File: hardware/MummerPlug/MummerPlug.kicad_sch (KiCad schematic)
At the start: 8 parts

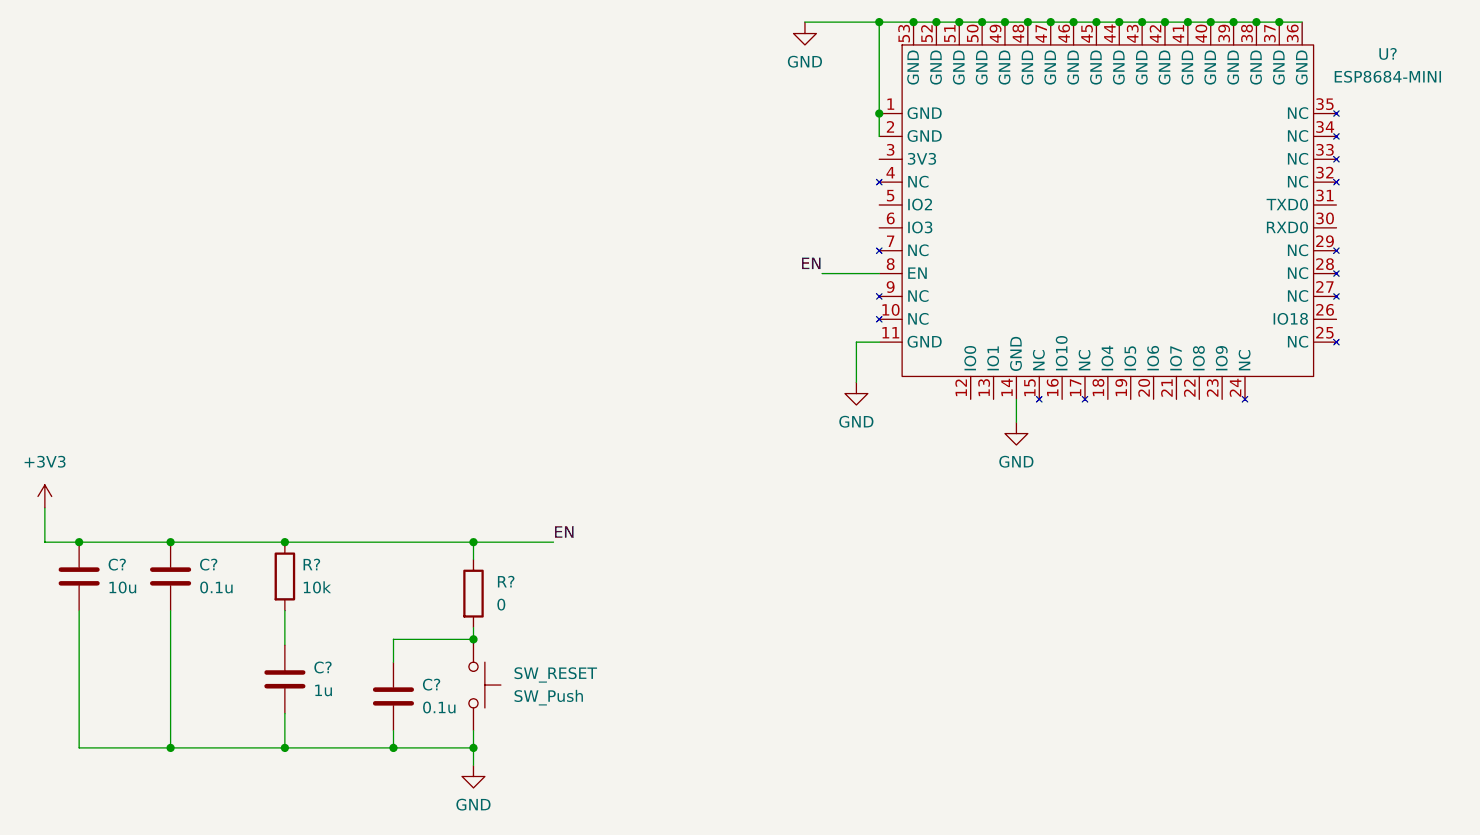
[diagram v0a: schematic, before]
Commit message: Cleaned up and add plug circuit
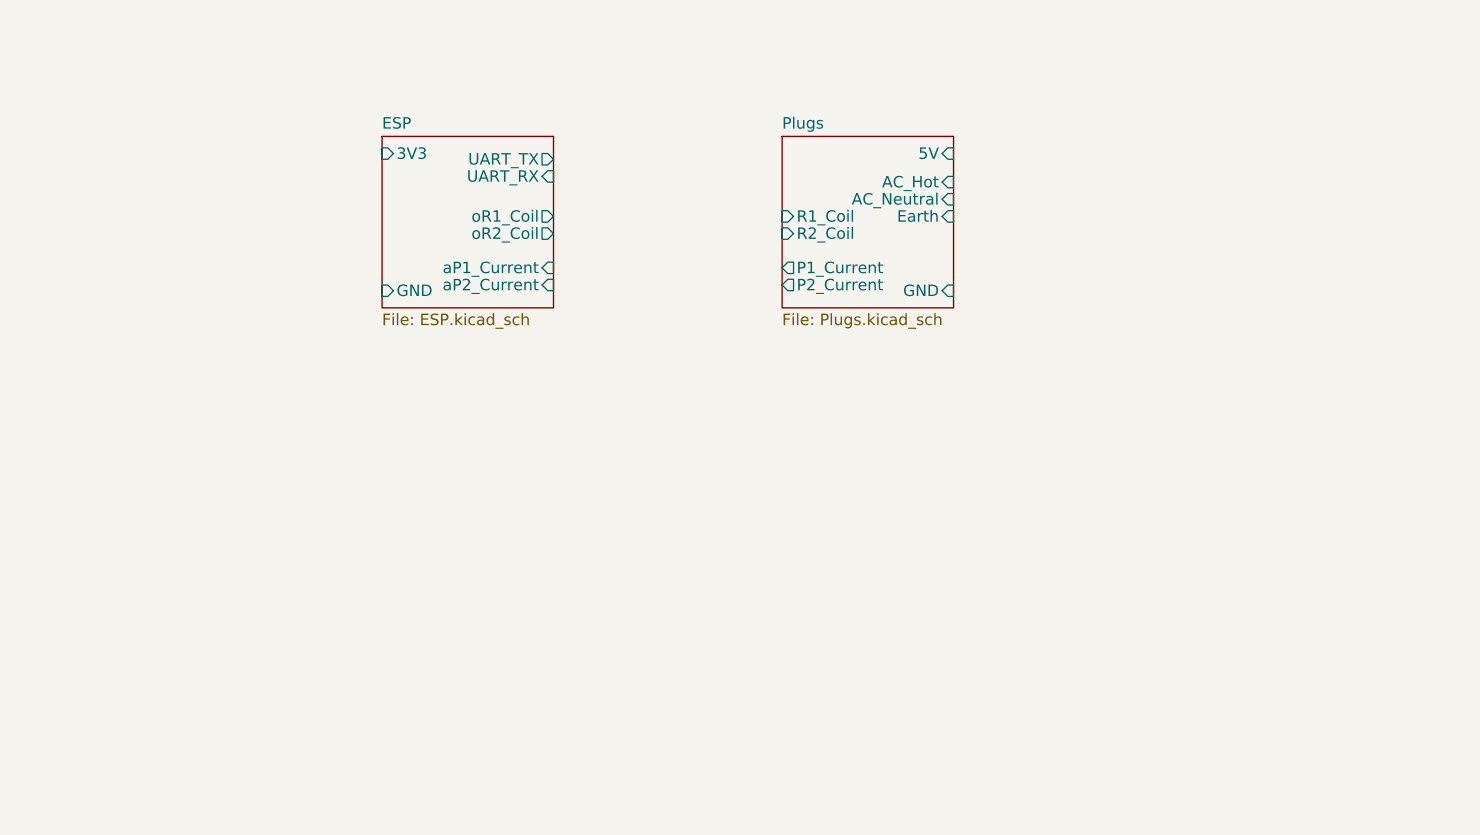
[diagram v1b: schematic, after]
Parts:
- removed C?: 1u, symbol Device:C
- removed C? (x2): 0.1u, symbol Device:C
- removed C?: 10u, symbol Device:C
- removed R?: 0, symbol Device:R
- removed R?: 10k, symbol Device:R
- removed SW_RESET: SW_Push, symbol Switch:SW_Push
- removed U?: ESP8684-MINI, symbol Mummerplug:ESP8684-MINI
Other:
- added sheet ESP (ESP.kicad_sch)
- added sheet Plugs (Plugs.kicad_sch)
